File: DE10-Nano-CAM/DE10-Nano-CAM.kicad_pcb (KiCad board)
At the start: 4 copper layers, 65.4 x 103.6 mm, 29 parts, among them J1 DF40C-100DS-0.4V_51_, J2 DF40C-100DS-0.4V_51_, J3 MEM2075-00-140-01-A, J4 HDMI_A, J5 52271-1579

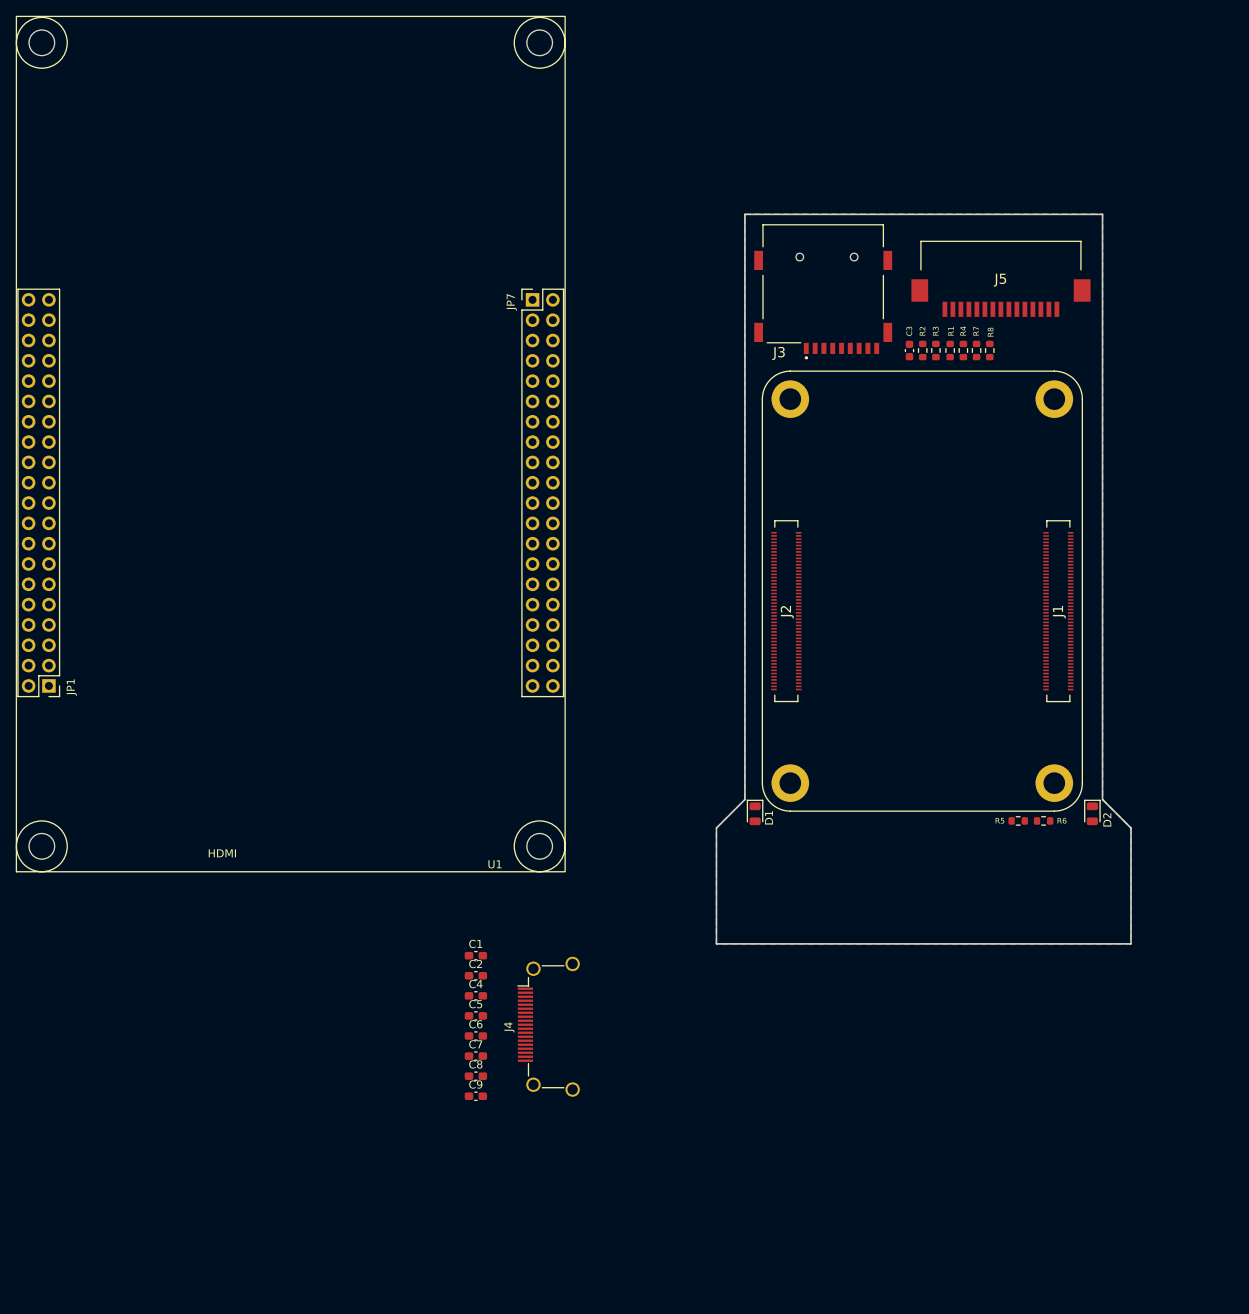
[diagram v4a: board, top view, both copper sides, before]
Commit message: changed initial pcb layout
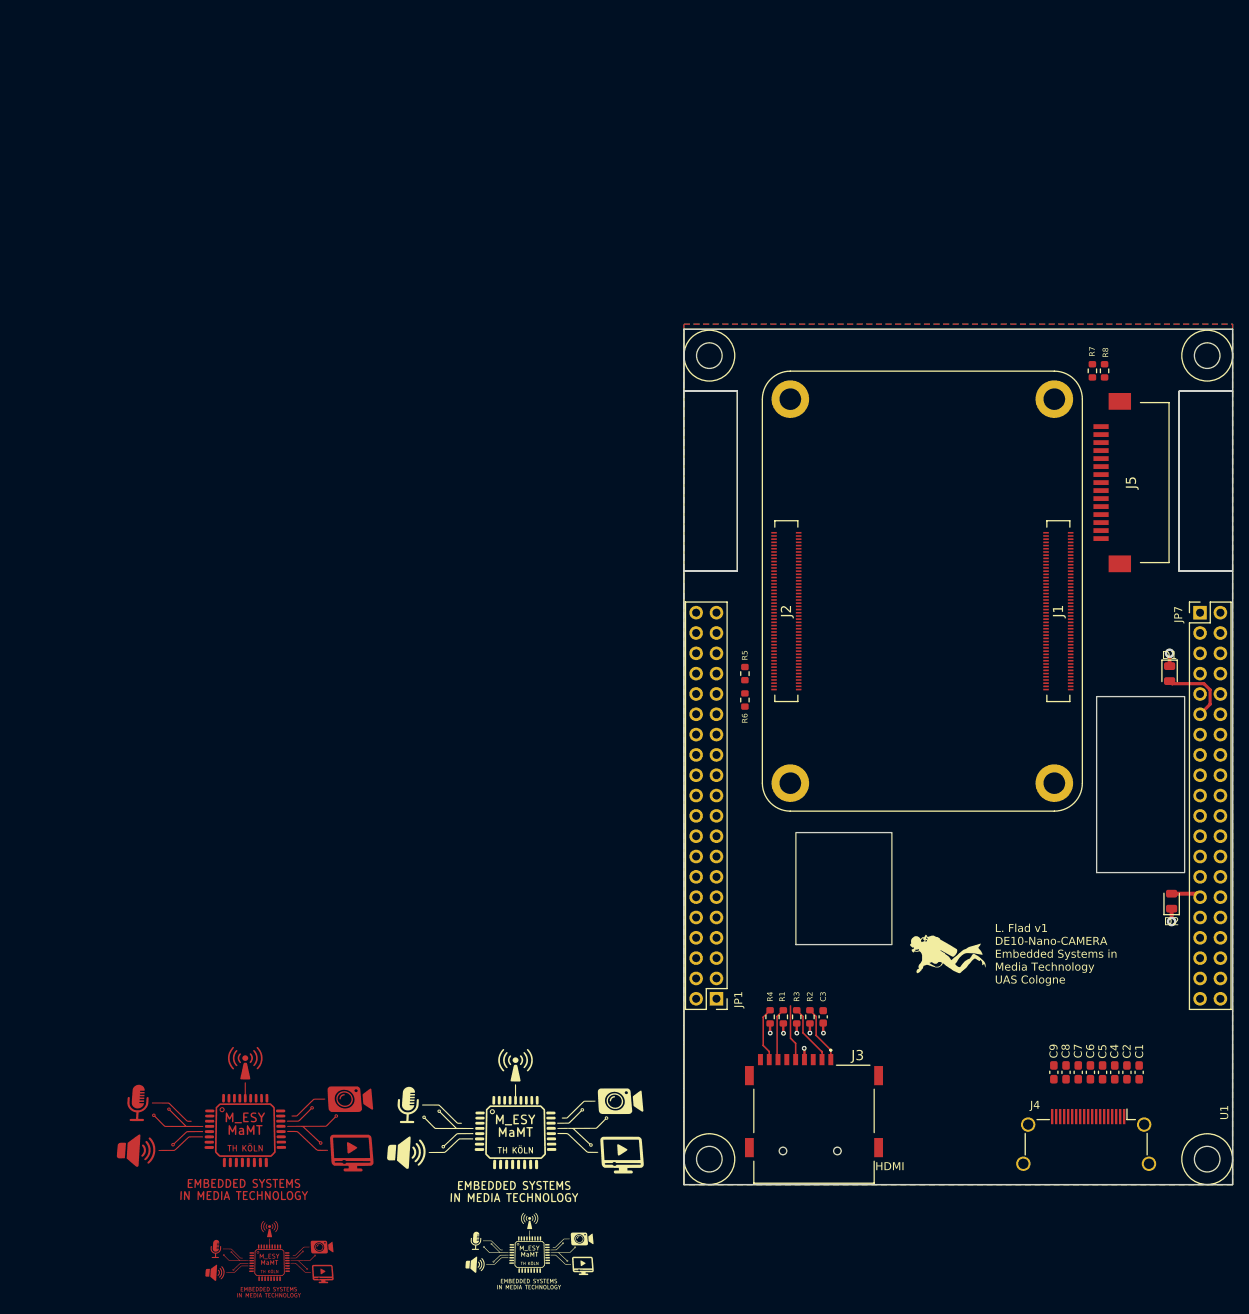
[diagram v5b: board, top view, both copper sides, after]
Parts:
- added G***: LOGO, LOGO, F.Cu at (58.7, 174.8)
- added G***: LOGO, LOGO, F.Cu at (91.2, 173.7)
- added G***: LOGO, LOGO, F.Cu at (143.5, 136.1)
- added G***: LOGO, LOGO, F.Cu at (89.4, 158.5)
- added G***: LOGO, LOGO, F.Cu at (55.6, 158.2)
- moved J3 103.7 mm to (126.7, 156.7), turned to 0 degrees
- moved U1 92.1 mm to (175.9, 161.8)
- moved R4 86.7 mm to (121.3, 144.0), turned to -90 degrees
- moved R1 85.9 mm to (122.9, 144.0), turned to -90 degrees
- moved R3 85.1 mm to (124.6, 144.0), turned to -90 degrees
- moved R2 84.5 mm to (126.2, 144.0), turned to -90 degrees
- moved C1 84.2 mm to (167.4, 150.9), turned to -90 degrees
- moved C3 84.0 mm to (127.9, 144.0), turned to -90 degrees
- moved C2 82.3 mm to (165.9, 150.9), turned to -90 degrees
- moved C4 80.4 mm to (164.3, 150.9), turned to -90 degrees
- moved C5 78.7 mm to (162.8, 150.9), turned to -90 degrees
- moved C6 77.0 mm to (161.3, 150.9), turned to -90 degrees
- moved C7 75.3 mm to (159.8, 150.9), turned to -90 degrees
- moved C8 73.8 mm to (158.3, 150.9), turned to -90 degrees
- moved C9 72.3 mm to (156.7, 150.9), turned to -90 degrees
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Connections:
- C3 pad 2: +3.3V -> /+5V_DE10
- D1 pad 1: +5V -> /+5V_DE10
- D2 pad 1: +3.3V -> /+5V_DE10
- R1 pad 2: +3.3V -> /+5V_DE10
- R2 pad 2: +3.3V -> /+5V_DE10
- R3 pad 2: +3.3V -> /+5V_DE10
- R4 pad 2: +3.3V -> /+5V_DE10
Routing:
- net /+5V_DE10: track 0.00 -> 18.9 mm, vias 0 -> 7
- net /SD_DAT3: track 0.00 -> 7.52 mm
- net /SD_DAT2: track 0.00 -> 7.25 mm
- net /SD_CLK: track 0.00 -> 6.97 mm
- net /DATA_PullUp: track 0.00 -> 6.84 mm
- net /SD_DAT0: track 0.00 -> 6.54 mm
- net /+3.3V_DE10: track 0.00 -> 3.74 mm
- net +3.3V: track 0.00 -> 1.43 mm, vias 0 -> 1
- added copper zone on In1.Cu, net +3.3V
- removed copper zone on In1.Cu, net +3V3
- removed copper zone on In2.Cu, net +5V
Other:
- board size 65.4 x 103.6 mm -> 68.6 x 106.9 mm
- board text added: "L. Flad v1 DE10-Nano-CAMERA Embedded Systems in Media Technology UAS Cologne"

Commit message: final v1 PCB design. Missing via stitching
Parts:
- removed the G*** at (58.7, 174.8)
- removed the G*** at (91.2, 173.7)
- C1, C2, C4, C5, C6, C7, C8, C9: footprint Capacitor_SMD:C_0603_1608Metric_Pad1.08x0.95mm_HandSolder -> Capacitor_SMD:C_0402_1005Metric
- R1, R2, R3, R4: footprint Resistor_SMD:R_0603_1608Metric -> Resistor_SMD:R_0402_1005Metric
- R5, R6: moved to B.Cu
- moved G*** 11.8 mm to (144.9, 124.4)
- moved G*** 2.77 mm to (89.5, 155.7)
- moved C9 2.75 mm to (159.4, 151.4)
- moved C8 2.21 mm to (160.4, 151.4)
- moved C7 1.69 mm to (161.4, 151.4)
- moved R7 1.58 mm to (163.1, 63.2)
- moved R8 1.49 mm to (161.6, 63.2)
- moved C1 1.21 mm to (166.3, 151.4)
- moved C6 1.15 mm to (162.3, 151.4)
- moved C5 0.71 mm to (163.4, 151.4)
- moved C2 0.71 mm to (165.3, 151.4)
- moved C4 0.46 mm to (164.3, 151.4)
- moved R5 0.34 mm to (117.8, 101.1)
- moved R6 0.34 mm to (117.8, 104.4)
- moved U1 0.06 mm to (175.8, 161.8)
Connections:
- C3 pad 2: /+5V_DE10 -> +3.3V
- D1 pad 1: /+5V_DE10 -> +5V
- D2 pad 1: /+5V_DE10 -> +3.3V
- J2 pad 84: +3V3 -> +3.3V
- J2 pad 86: +3V3 -> +3.3V
- R1 pad 2: /+5V_DE10 -> +3.3V
- R2 pad 2: /+5V_DE10 -> +3.3V
- R3 pad 2: /+5V_DE10 -> +3.3V
- R4 pad 2: /+5V_DE10 -> +3.3V
- U1 pad 1_1: /DATA_0 -> unconnected-(U1-Pad1_1)
- U1 pad 1_10: /DATA_8 -> unconnected-(U1-Pad1_10)
- U1 pad 1_13: /DATA_9 -> /DATA_3
- U1 pad 1_14: /DATA_10 -> /DATA_4
- U1 pad 1_15: /DATA_11 -> /DATA_5
- U1 pad 1_16: /DATA_12 -> /DATA_6
- U1 pad 1_17: /DATA_14 -> /DATA_7
- U1 pad 1_18: /DATA_13 -> /DATA_8
- U1 pad 1_19: /DATA_15 -> /DATA_9
- U1 pad 1_2: /PIXEL_CLK -> unconnected-(U1-Pad1_2)
- U1 pad 1_20: /VSYNC -> /DATA_10
- U1 pad 1_21: /DATA_16 -> /DATA_11
- U1 pad 1_22: /DATA_17 -> /DATA_12
- U1 pad 1_23: /DATA_18 -> /DATA_13
- U1 pad 1_24: /DATA_19 -> /DATA_20
- U1 pad 1_25: /HSYNC -> /DATA_19
- U1 pad 1_26: /DATA_20 -> /DATA_18
- U1 pad 1_3: /DATA_1 -> unconnected-(U1-Pad1_3)
- U1 pad 1_33: /DATA_22 -> /DATA_17
- U1 pad 1_34: /DATA_23 -> /DATA_16
- U1 pad 1_35: /DATA_24 -> /DATA_15
- U1 pad 1_36: /DATA_25 -> /DATA_14
- U1 pad 1_37: /DATA_26 -> /DATA_33
- U1 pad 1_38: /DATA_27 -> /DATA_32
- U1 pad 1_39: /DATA_28 -> /DATA_31
- U1 pad 1_4: /DATA_2 -> unconnected-(U1-Pad1_4)
- U1 pad 1_40: unconnected-(U1-Pad1_40) -> /DATA_30
- U1 pad 1_5: /DATA_3 -> /DATA_0
- U1 pad 1_6: /DATA_4 -> unconnected-(U1-Pad1_6)
- U1 pad 1_7: /DATA_5 -> /DATA_1
- U1 pad 1_8: /DATA_6 -> /DATA_2
- U1 pad 1_9: /DATA_7 -> unconnected-(U1-Pad1_9)
- U1 pad 7_10: unconnected-(U1-Pad7_10) -> /DATA_28
- U1 pad 7_12: unconnected-(U1-Pad7_12) -> GND
- U1 pad 7_15: unconnected-(U1-Pad7_15) -> /VSYNC
- U1 pad 7_16: unconnected-(U1-Pad7_16) -> /HSYNC
- U1 pad 7_2: /DATA_30 -> /PIXEL_CLK
- U1 pad 7_3: /DATA_31 -> /DATA_23
- U1 pad 7_30: unconnected-(U1-Pad7_30) -> GND
- U1 pad 7_4: /DATA_32 -> /DATA_22
- U1 pad 7_5: /DATA_33 -> /DATA_25
- U1 pad 7_6: unconnected-(U1-Pad7_6) -> /DATA_24
- U1 pad 7_7: unconnected-(U1-Pad7_7) -> /DATA_27
- U1 pad 7_8: unconnected-(U1-Pad7_8) -> /DATA_26
- U1 pad 7_9: unconnected-(U1-Pad7_9) -> /DATA_29
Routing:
- net +5V: track 0.00 -> 132.8 mm, vias 0 -> 10
- net /SD_CMD: track 0.00 -> 110.0 mm, vias 0 -> 2
- net /SD_DAT0: track 6.54 -> 113.0 mm
- net /DATA_PullUp: track 6.84 -> 113.0 mm
- net /SD_CLK: track 6.97 -> 113.0 mm
- net /SD_DAT2: track 7.25 -> 110.0 mm, vias 0 -> 2
- net /SD_DAT3: track 7.52 -> 110.0 mm, vias 0 -> 2
- net GND: track 0.00 -> 86.2 mm, vias 0 -> 47
- net /+3.3V_DE10: track 3.74 -> 73.7 mm, vias 0 -> 2
- net /DATA_32: track 0.00 -> 65.4 mm
- net /DATA_15: track 0.00 -> 65.4 mm
- net /DATA_0: track 0.00 -> 65.4 mm
- net /DATA_14: track 0.00 -> 65.4 mm
- net /DATA_16: track 0.00 -> 65.4 mm
- net /DATA_33: track 0.00 -> 65.4 mm
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- added copper zone on In2.Cu, net +3.3V
- added copper zone on In1.Cu, net GND
- removed copper zone on In1.Cu, net +3.3V
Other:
- outline, holes or cut-outs redrawn
- board text added: "TODO Ckeck lengths Set Via Stitching between Traces"
- board text added: "ULX5M-GS"

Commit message: uplead ready to order PCBs
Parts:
- removed the G*** at (55.6, 158.2)
- moved G*** 66.5 mm to (153.4, 137.4)
- moved G*** 37.4 mm to (144.5, 161.8)
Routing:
- net +5V: track 132.8 -> 133.8 mm
- net GND: track 86.2 -> 85.5 mm, vias 47 -> 932
- net /PIXEL_CLK: track 63.7 -> 64.4 mm
- added copper zone on In2.Cu, net GND
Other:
- board text added: "CAMERA"
- board text added: "{ "ViaStitching": "0.2", "stitch_zone_0": { "HSpacing": "1", "VSpacing": "1", "HOffset": "0", "VOffset": "0", "Clearance": "0", "Randomize": false } }"
- board text added: "{ "ViaStitching": "0.2", "stitch_zone_0": { "HSpacing": "1", "VSpacing": "1", "HOffset": "0", "VOffset": "0", "Clearance": "0.1", "Randomize": false } }"
- board text added: "{ "ViaStitching": "0.2", "stitch_zone_0": { "HSpacing": "1", "VSpacing": "1", "HOffset": "1", "VOffset": "1", "Clearance": "0.2", "Randomize": false } }"
- board text added: "{ "ViaStitching": "0.2", "stitch_zone_0": { "HSpacing": "1", "VSpacing": "1", "HOffset": "5", "VOffset": "5", "Clearance": "2", "Randomize": false } }"
- board text added: "{ "ViaStitching": "0.2", "stitch_zone_0": { "HSpacing": "1", "VSpacing": "3", "HOffset": "0", "VOffset": "0", "Clearance": "0", "Randomize": false } }"
- board text added: "{ "ViaStitching": "0.2", "stitch_zone_0": { "HSpacing": "1.27", "VSpacing": "1.27", "HOffset": "0", "VOffset": "0", "Clearance": "0.2", "Randomize": false } }"
- board text added: "{ "ViaStitching": "0.2", "stitch_zone_0": { "HSpacing": "3", "VSpacing": "3", "HOffset": "0", "VOffset": "0", "Clearance": "3", "Randomize": false } }"
- board text added: "{ "ViaStitching": "0.2", "stitch_zone_0": { "HSpacing": "5", "VSpacing": "5", "HOffset": "0", "VOffset": "0", "Clearance": "0.1", "Randomize": false } }"
- board text added: "{ "ViaStitching": "0.2", "stitch_zone_0": { "HSpacing": "5", "VSpacing": "5", "HOffset": "5", "VOffset": "5", "Clearance": "2", "Randomize": false } }"
- board text added: "{ "ViaStitching": "0.2", "stitch_zone_0": { "HSpacing": "5", "VSpacing": "5", "HOffset": "5", "VOffset": "5", "Clearance": "5", "Randomize": false } }"
- board text removed: "TODO Ckeck lengths Set Via Stitching between Traces"
